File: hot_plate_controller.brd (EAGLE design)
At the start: 100 x 34 mm, 8 parts, among them J3 B4B-PH-K-S(LF)(SN), J5 1862042, J6 1862042, J7 1862042, U1 WEMOS_LOLIN32, U2 MAX6675

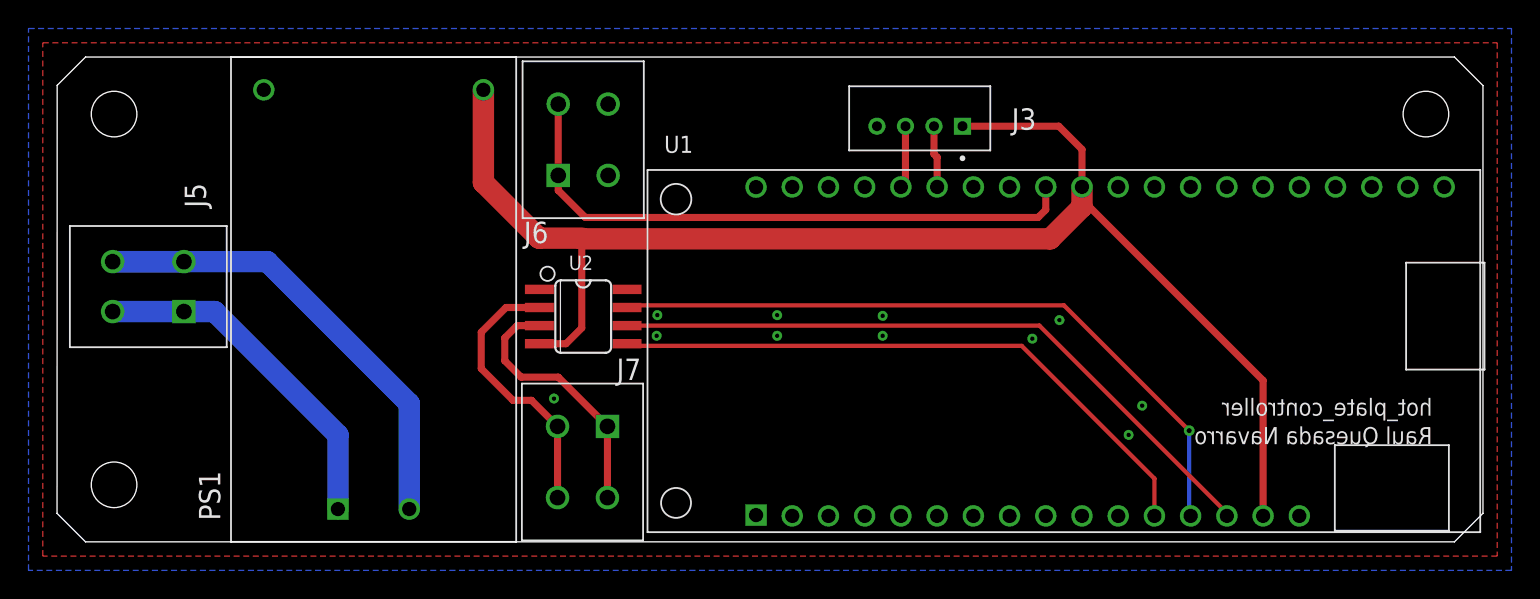
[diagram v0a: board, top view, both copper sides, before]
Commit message: - Add MotionLab logo. - Add separated power planes on AC side. - Add high voltage symbol. - place all texts in the right side with the right rotation. - add markings for SSR, thermocouple, i2c and AC in the hot plate board. - add a second connector for AC, just in case is needed to use as bridge. - add second i2c port. - add vias to communicate power planes.
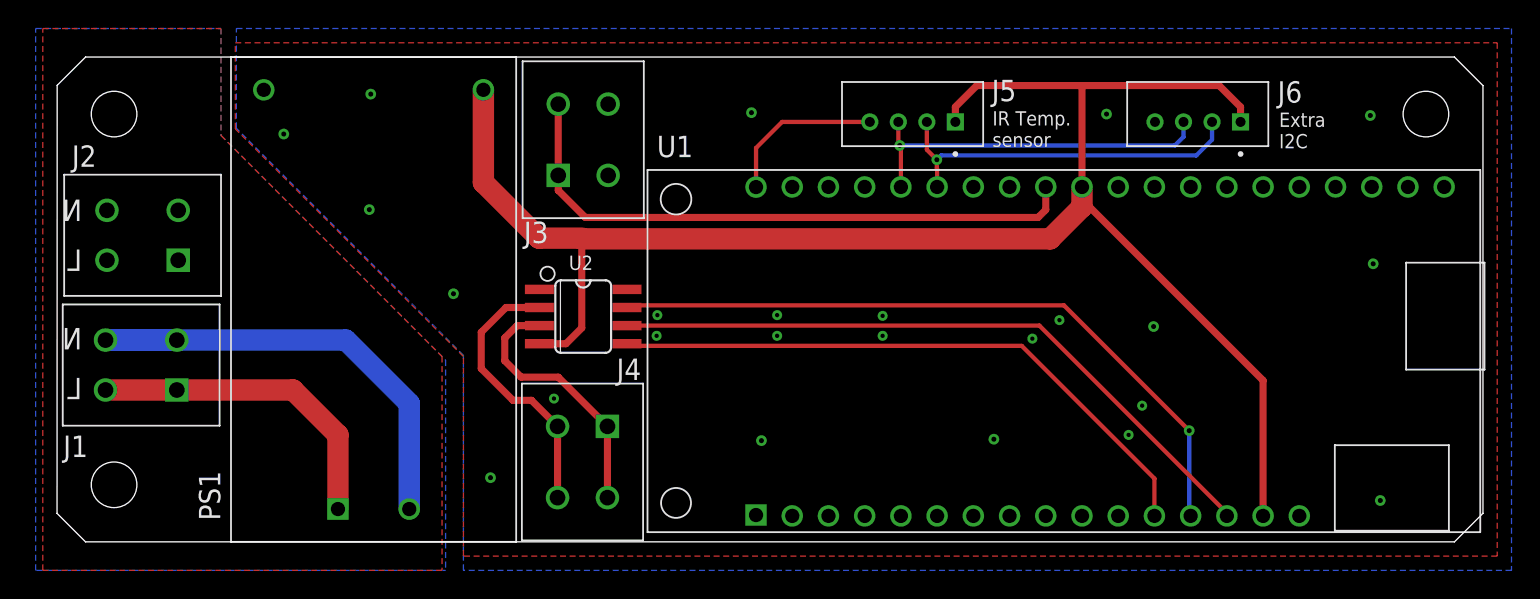
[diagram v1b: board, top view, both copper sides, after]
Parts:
- added J1, J2: 1862042, RE_hot_plate_controller:PHOENIX_1862042
- added U$2: (no value), ML_common:HIGH_VOLTAGE_LOGO_10MM
- J3: value B4B-PH-K-S(LF)(SN) -> 1862042; device RE_hot_plate_controller:JST_B4B-PH-K-S(LF)(SN) -> RE_hot_plate_controller:PHOENIX_1862042
- J5, J6: value 1862042 -> B4B-PH-K-S(LF)(SN); device RE_hot_plate_controller:PHOENIX_1862042 -> RE_hot_plate_controller:JST_B4B-PH-K-S(LF)(SN)
- moved J5 54.9 mm to (60.0, 30.0), turned to 0 degrees
- moved J6 43.1 mm to (80.0, 30.0)
- moved J3 23.6 mm to (36.9, 28.2)
- renumbered J7 to J4
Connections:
- removed net N$1: J5.1, J5.2, PS1.1
- removed net N$3: J5.3, J5.4, PS1.2
- new net AC_L: J1.1, J1.2, J2.1, J2.2, PS1.1
- new net AC_N: J1.3, J1.4, J2.3, J2.4, PS1.2
- net +5V: now also J5.1, J6.1; no longer J3.1
- net GND: now also J3.3, J5.4; no longer J6.3
- net I2C_SCL: now also J5.3, J6.3; no longer J3.3
- net I2C_SDA: now also J5.2, J6.2; no longer J3.2
- net SSR: now also J3.1, J3.2; no longer J6.1, J6.2
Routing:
- net N$3: track 37.3 -> 0.00 mm
- net AC_N: track 0.00 -> 35.5 mm
- net N$1: track 24.6 -> 0.00 mm
- net AC_L: track 0.00 -> 22.8 mm
- net I2C_SDA: track 4.35 -> 26.0 mm, vias 0 -> 1
- net I2C_SCL: track 4.39 -> 25.8 mm, vias 0 -> 1
- net +5V: track 101.1 -> 119.9 mm
- net GND: track 0.00 -> 11.5 mm, vias 11 -> 24
- added copper zone on layer 1, net AC_L
- added copper zone on layer 16, net AC_N
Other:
- board text added: "+"
- board text added: "-"
- board text added: "AC"
- board text added: "Extra I2C"
- board text added: "GND"
- board text added: "IR Temp. sensor"
- board text added: "L"
- board text added: "N"
- board text added: "R"
- board text added: "SSR"
- board text added: "Solid State Relay"
- board text added: "Thermocouple"
- board text added: "Yl"
